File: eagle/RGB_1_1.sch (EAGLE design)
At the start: 16 parts, among them X1 RGB, X2 Buzzer

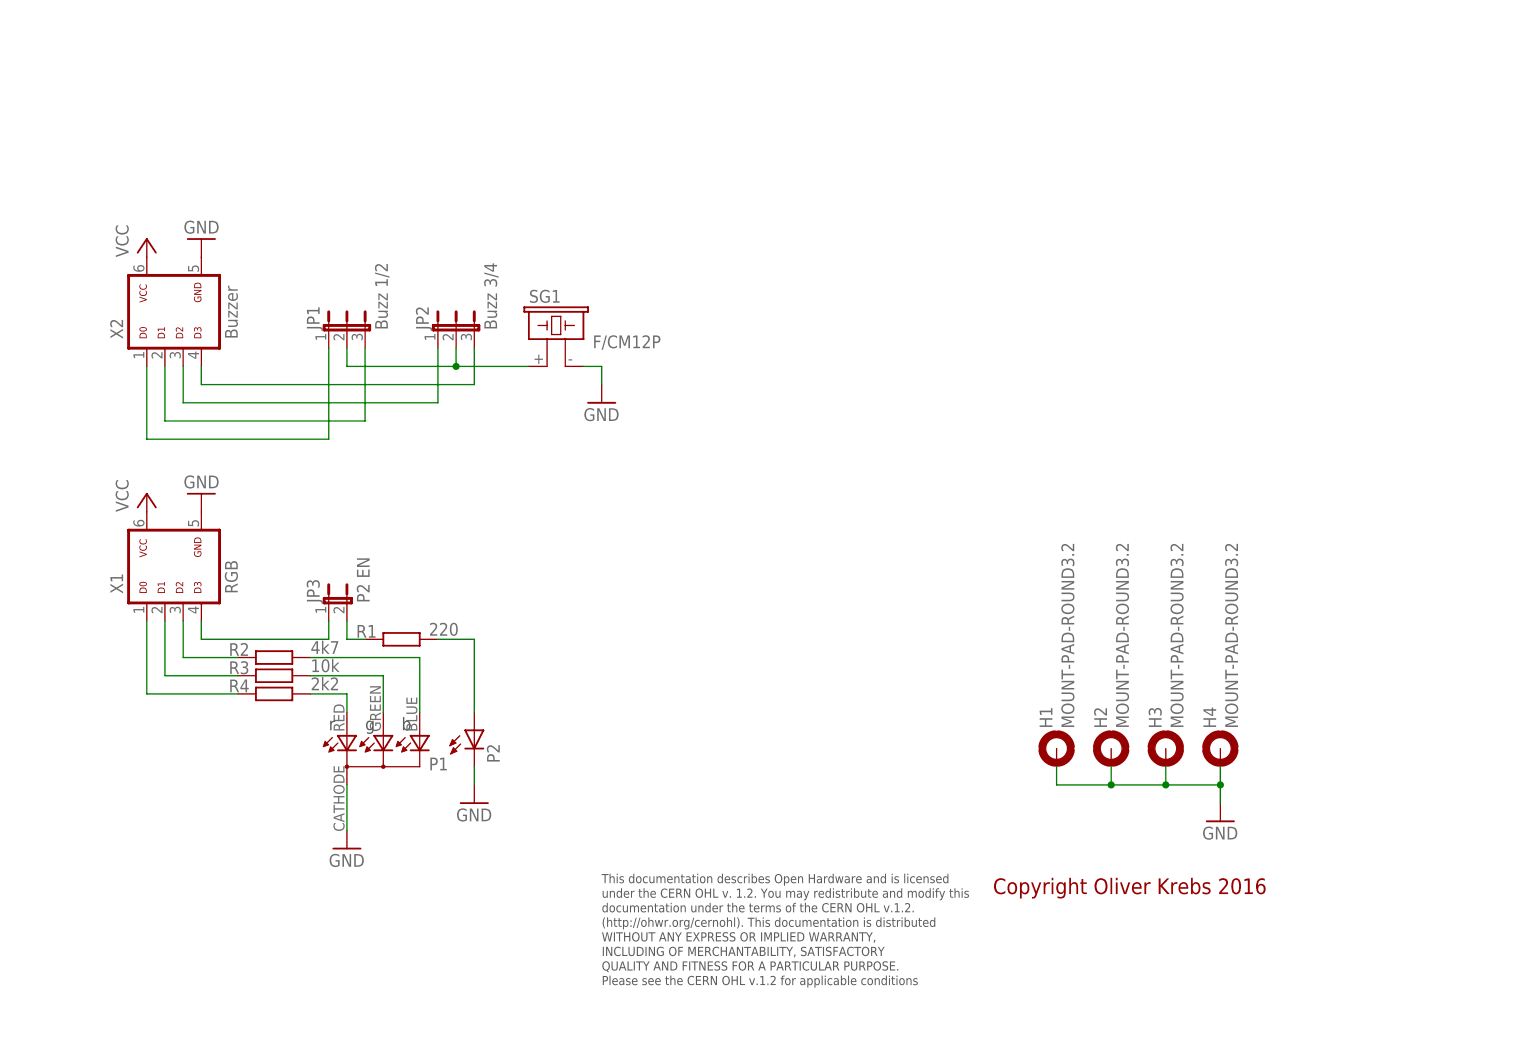
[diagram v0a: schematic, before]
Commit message: Add new tetra-Board and arduino files
Add AMP_1_0, AVC_1_0, D18_1_1, IOP_1_2, MIC_1_0, PIN_1_1, POT_1_0, PWA_1_0, PWR_1_0, RGF 2.0, SOC_2_0, VLT_1_0
Add mex_nano_shield_keyboard, mex_nano_shied_numbers

New arduino projects
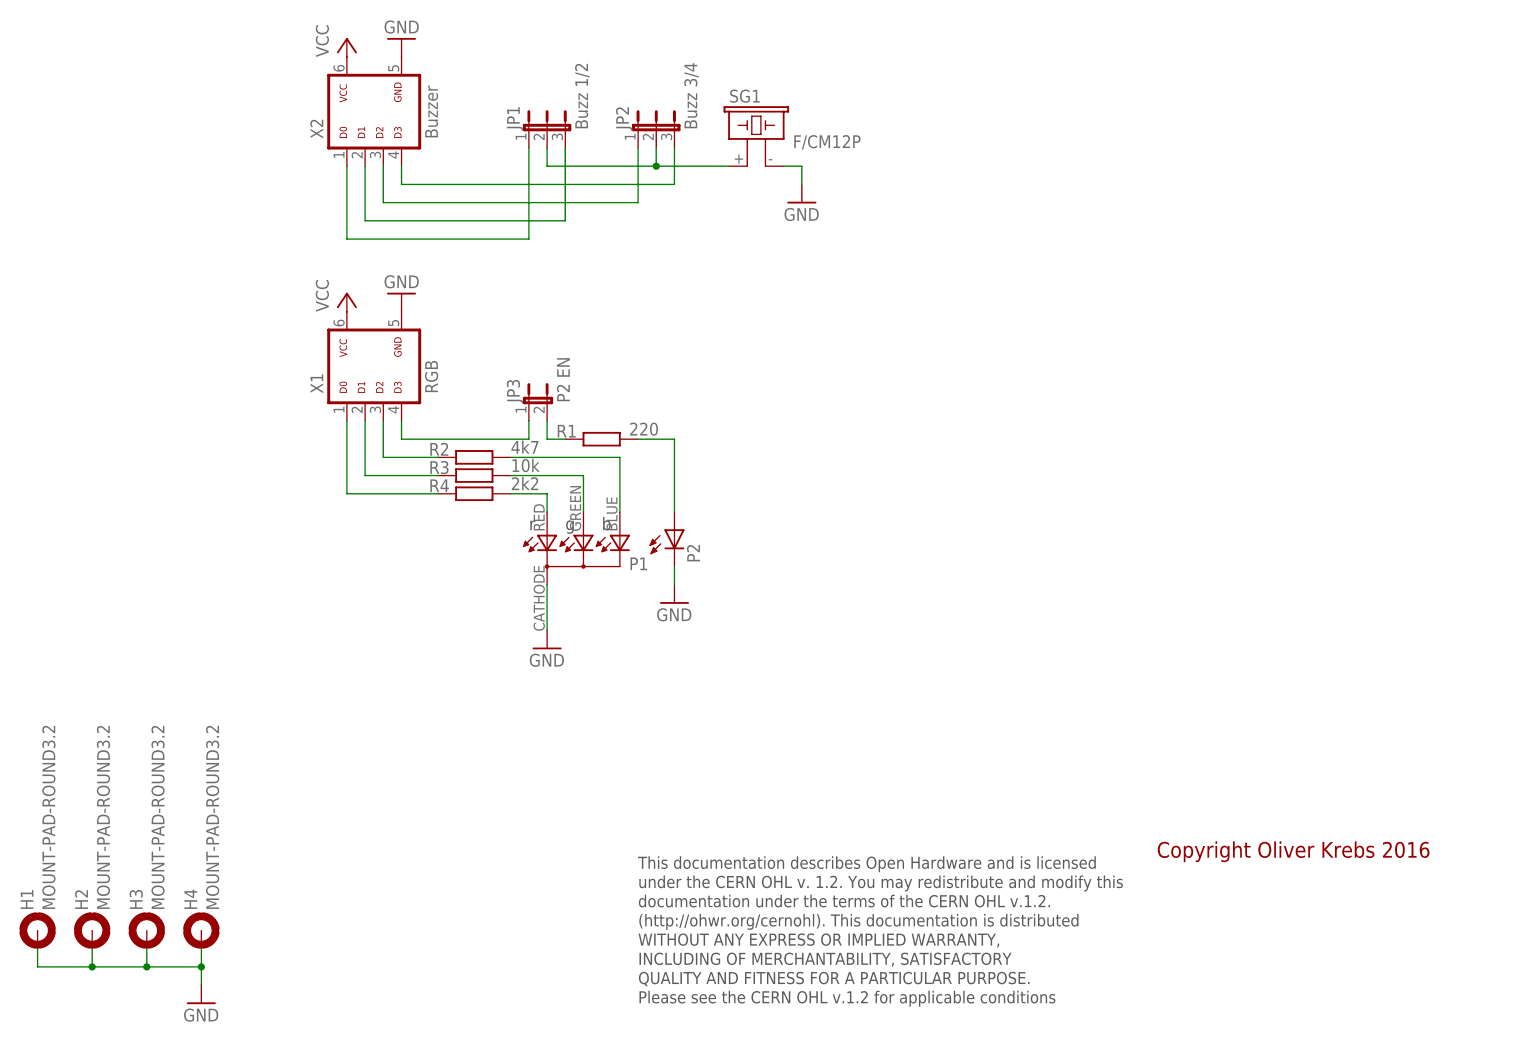
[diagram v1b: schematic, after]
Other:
- moved on the sheet: H1, H2, H3, H4, JP1, JP2, JP3, P1, P2, R1, R2, R3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
